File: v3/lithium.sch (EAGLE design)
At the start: 53 parts, among them J1 batt, J2 battery, J3 motor, U1 TPS61088VQFN20, U1_C22 8.2nF, U1_CBST 100nF, U1_CCOMP 680PF, U1_CCOMP2 36pF, U1_CIN 0.47uF, U1_CIN2 100nF, U1_COUT 0.47uF, U1_CVCC 1uF, U1_L1 DR73-1R0-R, U1_RCOMP 38.3K Ohms, U1_RFBB 118K Ohms, U1_RFBT 470K Ohms, U1_RLIM 102K Ohms, U1_RT 261K Ohms, U4 TPS2113APWR, U4_C3 0.1uF, U4_C4 0.1uF, U4_RPG 100K Ohms, U5 MCP73833-FCI/UN, U5_C1 1.0uF, U5_C2 1.0uF, U5_R1 1K Ohm, U6 TPS61230A, U6_CBST 10 nF, U6_CFF 10pF, U6_CIN 22uF, U6_COUT 22uF, U6_RFBB 100K Ohms, U6_RFBT 316K Ohms

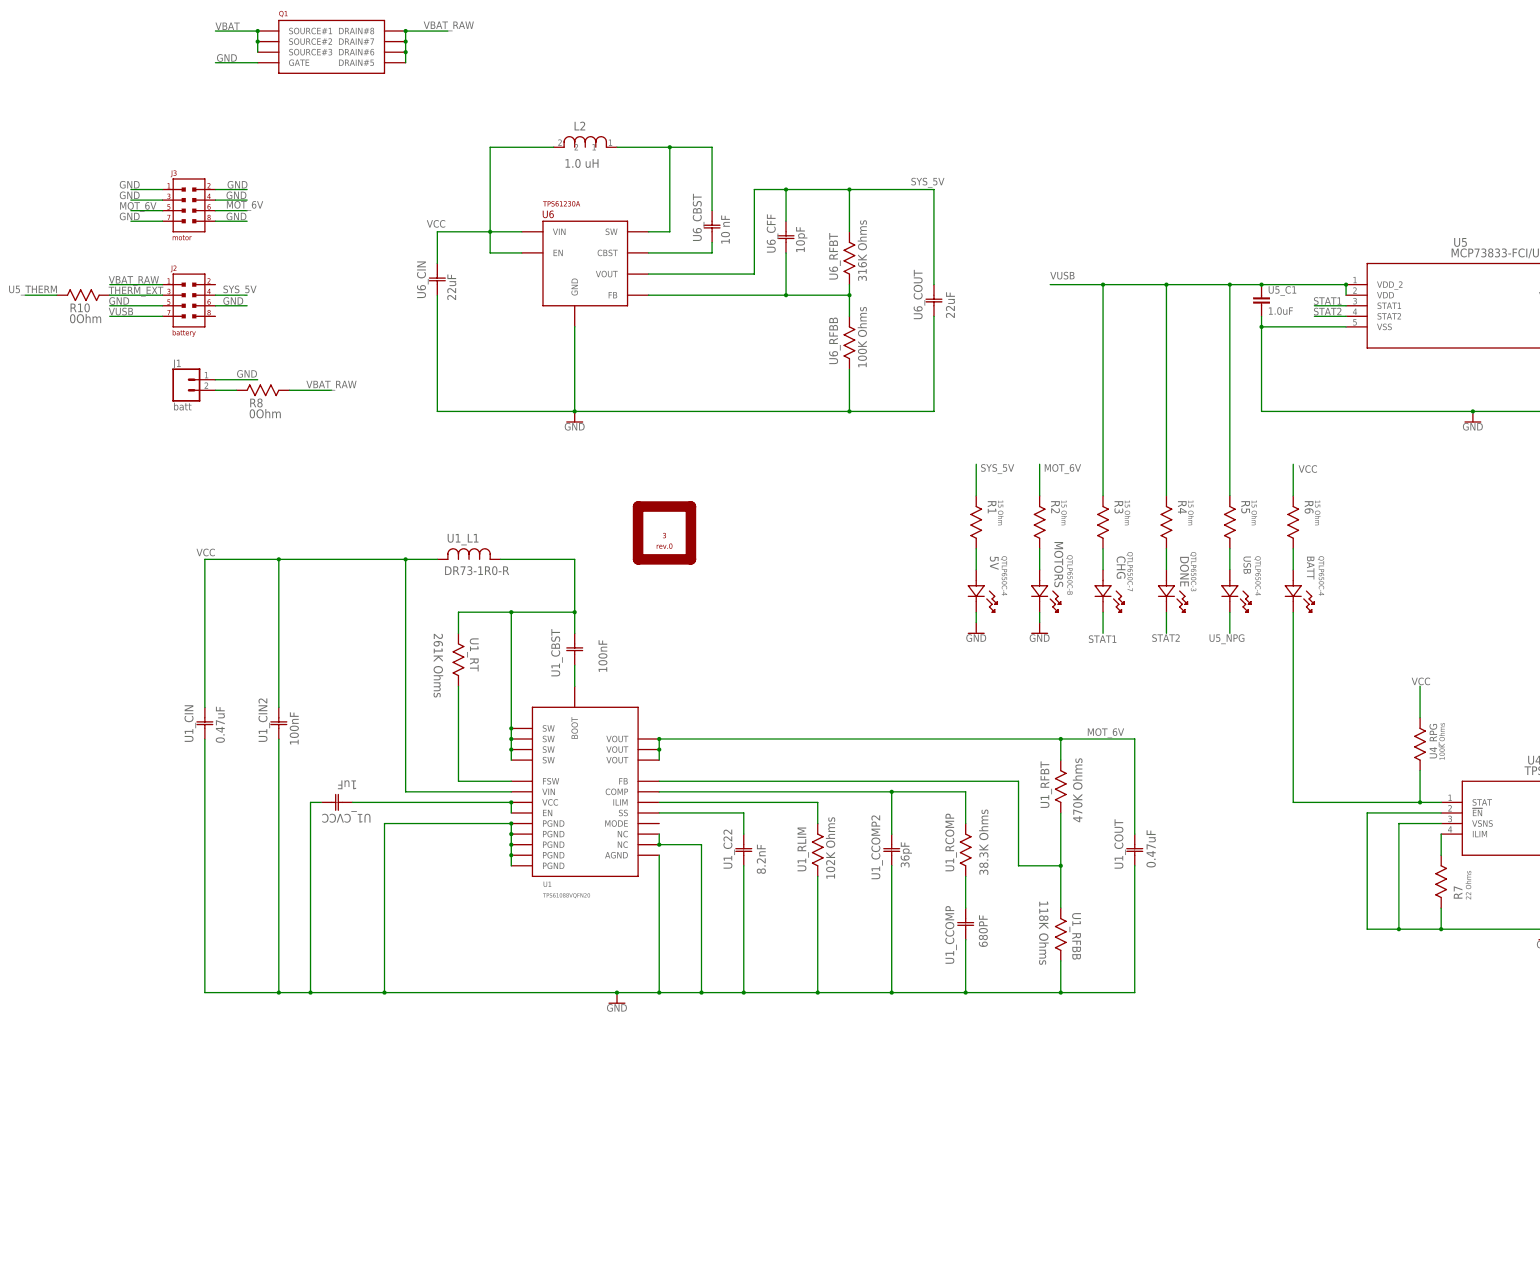
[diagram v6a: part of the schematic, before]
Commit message: Lithium with ATTiny84 for ADC.
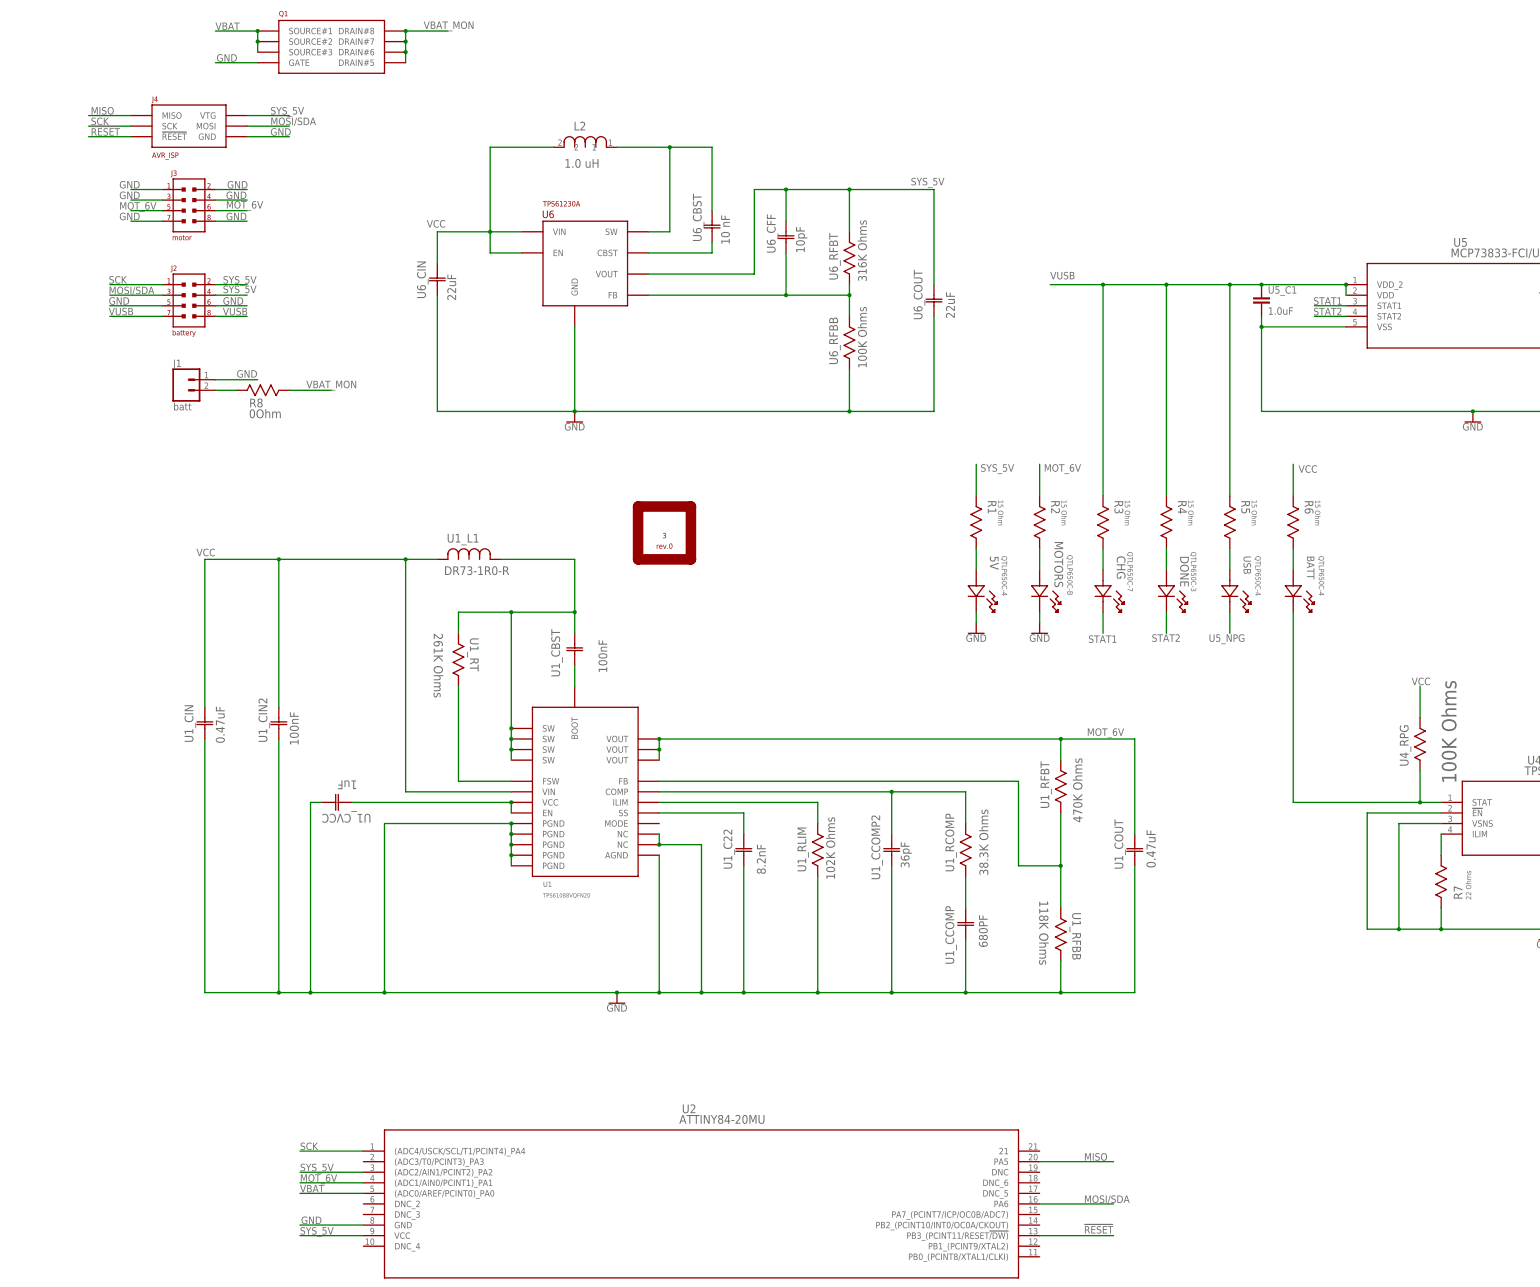
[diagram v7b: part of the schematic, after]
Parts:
- removed R10: 0Ohm, Vishay_By_element14_Batch_1:CRCW08050000Z0EB
- added J4: AVR_ISP, 32bits:AVR_ISP
- added U2: ATTINY84-20MU, 32bits:ATTINY84-20MU
- U4_RPG: device Vishay_By_element14_Batch_1:CRCW0603100KFKEA -> Vishay_By_element14_Batch_1:CRCW1206100KFKEA
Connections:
- removed net THERM_EXT: J2.3, R10.1
- removed net VBAT_RAW: J2.1, Q1.DRAIN#5, Q1.DRAIN#6, Q1.DRAIN#7, Q1.DRAIN#8, R8.1
- new net !RESET: J4.!RESET, U2.PB3_(PCINT11/RESET!/DW)
- new net MISO: J4.MISO, U2.PA5
- new net MOSI/SDA: J2.3, J4.MOSI, U2.PA6
- new net SCK: J2.1, J4.SCK, U2.(ADC4/USCK/SCL/T1/PCINT4)_PA4
- new net VBAT_MON: Q1.DRAIN#5, Q1.DRAIN#6, Q1.DRAIN#7, Q1.DRAIN#8, R8.1
- net GND: now also J4.GND, U2.GND
- net MOT_6V: now also U2.(ADC1/AIN0/PCINT1)_PA1
- net SYS_5V: now also J2.2, J4.VTG, U2.(ADC2/AIN1/PCINT2)_PA2, U2.VCC
- net U5_THERM: no longer R10.2
- net VBAT: now also U2.(ADC0/AREF/PCINT0)_PA0
- net VUSB: now also J2.8
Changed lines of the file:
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@@
 <part name="U4_C4" library="SparkFun-Capacitors" deviceset="0.1UF" device="-0402-16V-10%" value="0.1uF"/>
 <part name="BATT" library="Dialight_By_element14_Batch_1" deviceset="597-3311-407F" device="" value="QTLP650C-4"/>
-<part name="U4_RPG" library="Vishay_By_element14_Batch_1" deviceset="CRCW0603100KFKEA" device="" value="100K Ohms"/>
 <part name="U6" library="32bits" deviceset="TPS61230A" device=""/>
 <part name="L2" library="Bourns_By_element14_Batch_1" deviceset="PM1210-1R0J-RC" device="" value="1.0 uH"/>
@@
 <part name="S1" library="32bits" deviceset="SS312SAH4" device=""/>
 <part name="Q1" library="32bits" deviceset="SI7137DP" device=""/>
-<part name="R10" library="Vishay_By_element14_Batch_1" deviceset="CRCW08050000Z0EB" device="" value="0Ohm"/>
+<part name="U2" library="32bits" deviceset="ATTINY84-20MU" device=""/>
+<part name="J4" library="32bits" deviceset="AVR_ISP" device=""/>
+<part name="U4_RPG" library="Vishay_By_element14_Batch_1" deviceset="CRCW1206100KFKEA" device="" value="100K Ohms"/>
 </parts>
 <sheets>
@@
 <attribute name="NAME" x="264.922" y="105.0036" size="1.778" layer="95" ratio="10" rot="SR270"/>
 </instance>
-<instance part="U4_RPG" gate="A" x="292.1" y="53.34" smashed="yes" rot="R90">
-<attribute name="VALUE" x="298.0436" y="55.8038" size="1.27" layer="96" ratio="10" rot="SR90"/>
-<attribute name="NAME" x="296.1894" y="56.1086" size="1.778" layer="95" ratio="10" rot="SR90"/>
-</instance>
 <instance part="U6" gate="G$1" x="81.28" y="185.42"/>
 <instance part="L2" gate="A" x="83.82" y="203.2" smashed="yes">
@@
 <instance part="S1" gate="G$1" x="363.22" y="58.42" rot="R90"/>
 <instance part="Q1" gate="G$1" x="17.78" y="233.68"/>
-<instance part="R10" gate="A" x="-35.56" y="167.64" smashed="yes">
-<attribute name="VALUE" x="-32.5882" y="160.9344" size="2.1082" layer="96" ratio="10" rot="SR0"/>
-<attribute name="NAME" x="-32.5374" y="163.5506" size="2.0828" layer="95" ratio="10" rot="SR0"/>
-</instance>
+<instance part="U2" gate="A" x="35.56" y="-38.1"/>
+<instance part="J4" gate="A" x="-12.7" y="213.36"/>
+<instance part="U4_RPG" gate="A" x="292.1" y="53.34" rot="R90"/>
 </instances>
 <busses>
@@
 <label x="5.08" y="190.754" size="1.778" layer="95"/>
 </segment>
+<segment>
+<pinref part="U2" gate="A" pin="GND"/>
+<wire x1="38.1" y1="-55.88" x2="22.86" y2="-55.88" width="0.1524" layer="91"/>
+<label x="23.114" y="-55.626" size="1.778" layer="95"/>
+</segment>
+<segment>
+<pinref part="J4" gate="A" pin="GND"/>
+<wire x1="10.16" y1="205.74" x2="20.32" y2="205.74" width="0.1524" layer="91"/>
+<label x="15.748" y="205.994" size="1.778" layer="95"/>
+</segment>
 </net>
 <net name="SW" class="0">
@@
 </segment>
 <segment>
-<pinref part="U4_RPG" gate="A" pin="1"/>
 <wire x1="292.1" y1="66.04" x2="292.1" y2="73.66" width="0.1524" layer="91"/>
 <label x="290.068" y="73.914" size="1.778" layer="95"/>
+<pinref part="U4_RPG" gate="A" pin="1"/>
 </segment>
 <segment>
@@
 <label x="5.08" y="188.468" size="1.778" layer="95"/>
 </segment>
+<segment>
+<pinref part="U2" gate="A" pin="(ADC1/AIN0/PCINT1)_PA1"/>
+<wire x1="38.1" y1="-45.72" x2="22.86" y2="-45.72" width="0.1524" layer="91"/>
+<label x="22.86" y="-45.466" size="1.778" layer="95"/>
+</segment>
 </net>
 <net name="VBAT" class="0">
@@
 <junction x="12.7" y="231.14"/>
 <label x="2.54" y="231.394" size="1.778" layer="95"/>
+</segment>
+<segment>
+<pinref part="U2" gate="A" pin="(ADC0/AREF/PCINT0)_PA0"/>
+<wire x1="38.1" y1="-48.26" x2="22.86" y2="-48.26" width="0.1524" layer="91"/>
+<label x="22.86" y="-48.006" size="1.778" layer="95"/>
 </segment>
 </net>
@@
 <label x="-23.114" y="162.814" size="1.778" layer="95"/>
 </segment>
+<segment>
+<pinref part="J2" gate="A" pin="8"/>
+<wire x1="2.54" y1="162.56" x2="10.16" y2="162.56" width="0.1524" layer="91"/>
+<label x="4.318" y="162.814" size="1.778" layer="95"/>
+</segment>
 </net>
 <net name="U5_PROG" class="0">
@@
 <pinref part="U4" gate="A" pin="STAT"/>
 <wire x1="297.18" y1="45.72" x2="292.1" y2="45.72" width="0.1524" layer="91"/>
-<pinref part="U4_RPG" gate="A" pin="2"/>
 <wire x1="292.1" y1="53.34" x2="292.1" y2="45.72" width="0.1524" layer="91"/>
 <wire x1="261.62" y1="45.72" x2="292.1" y2="45.72" width="0.1524" layer="91"/>
 <junction x="292.1" y="45.72"/>
+<pinref part="U4_RPG" gate="A" pin="2"/>
 </segment>
 </net>
@@
 <label x="4.318" y="168.148" size="1.778" layer="95"/>
 </segment>
+<segment>
+<pinref part="J2" gate="A" pin="2"/>
+<wire x1="2.54" y1="170.18" x2="10.16" y2="170.18" width="0.1524" layer="91"/>
+<label x="4.318" y="170.434" size="1.778" layer="95"/>
+</segment>
+<segment>
+<pinref part="U2" gate="A" pin="VCC"/>
+<wire x1="38.1" y1="-58.42" x2="22.86" y2="-58.42" width="0.1524" layer="91"/>
+<label x="22.86" y="-58.166" size="1.778" layer="95"/>
+</segment>
+<segment>
+<pinref part="U2" gate="A" pin="(ADC2/AIN1/PCINT2)_PA2"/>
+<wire x1="38.1" y1="-43.18" x2="22.86" y2="-43.18" width="0.1524" layer="91"/>
+<label x="22.86" y="-42.926" size="1.778" layer="95"/>
+</segment>
+<segment>
+<pinref part="J4" gate="A" pin="VTG"/>
+<wire x1="10.16" y1="210.82" x2="20.32" y2="210.82" width="0.1524" layer="91"/>
+<label x="15.748" y="211.074" size="1.778" layer="95"/>
+</segment>
 </net>
 <net name="U1_VCC" class="0">
@@
 <wire x1="355.6" y1="165.1" x2="355.6" y2="157.48" width="0.1524" layer="91"/>
 </segment>
-<segment>
-<pinref part="R10" gate="A" pin="2"/>
-<wire x1="-35.56" y1="167.64" x2="-43.18" y2="167.64" width="0.1524" layer="91"/>
-<label x="-47.244" y="168.148" size="1.778" layer="95"/>
-</segment>
 </net>
 <net name="U4_ILIM" class="0">
@@
 </segment>
 </net>
-<net name="VBAT_RAW" class="0">
+<net name="VBAT_MON" class="0">
 <segment>
 <pinref part="Q1" gate="G$1" pin="DRAIN#5"/>
@@
 </segment>
 <segment>
+<pinref part="R8" gate="A" pin="1"/>
+<wire x1="20.32" y1="144.78" x2="30.48" y2="144.78" width="0.1524" layer="91"/>
+<label x="24.384" y="145.288" size="1.778" layer="95"/>
+</segment>
+</net>
+<net name="SCK" class="0">
+<segment>
+<pinref part="U2" gate="A" pin="(ADC4/USCK/SCL/T1/PCINT4)_PA4"/>
+<wire x1="38.1" y1="-38.1" x2="22.86" y2="-38.1" width="0.1524" layer="91"/>
+<label x="22.86" y="-37.846" size="1.778" layer="95"/>
+</segment>
+<segment>
+<pinref part="J4" gate="A" pin="SCK"/>
+<wire x1="-17.78" y1="208.28" x2="-27.94" y2="208.28" width="0.1524" layer="91"/>
+<label x="-27.432" y="208.534" size="1.778" layer="95"/>
+</segment>
+<segment>
 <pinref part="J2" gate="A" pin="1"/>
 <wire x1="-10.16" y1="170.18" x2="-22.86" y2="170.18" width="0.1524" layer="91"/>
 <label x="-23.114" y="170.434" size="1.778" layer="95"/>
 </segment>
-<segment>
-<pinref part="R8" gate="A" pin="1"/>
-<wire x1="20.32" y1="144.78" x2="30.48" y2="144.78" width="0.1524" layer="91"/>
-<label x="24.384" y="145.288" size="1.778" layer="95"/>
-</segment>
-</net>
-<net name="THERM_EXT" class="0">
+</net>
+<net name="!RESET" class="0">
+<segment>
+<pinref part="U2" gate="A" pin="PB3_(PCINT11/RESET!/DW)"/>
+<wire x1="200.66" y1="-58.42" x2="218.44" y2="-58.42" width="0.1524" layer="91"/>
+<label x="211.328" y="-57.912" size="1.778" layer="95"/>
+</segment>
+<segment>
+<pinref part="J4" gate="A" pin="!RESET"/>
+<wire x1="-17.78" y1="205.74" x2="-27.94" y2="205.74" width="0.1524" layer="91"/>
+<label x="-27.432" y="205.994" size="1.778" layer="95"/>
+</segment>
+</net>
+<net name="MOSI/SDA" class="0">
+<segment>
+<pinref part="U2" gate="A" pin="PA6"/>
+<wire x1="200.66" y1="-50.8" x2="218.44" y2="-50.8" width="0.1524" layer="91"/>
+<label x="211.328" y="-50.546" size="1.778" layer="95"/>
+</segment>
+<segment>
+<pinref part="J4" gate="A" pin="MOSI"/>
+<wire x1="10.16" y1="208.28" x2="20.32" y2="208.28" width="0.1524" layer="91"/>
+<label x="15.748" y="208.534" size="1.778" layer="95"/>
+</segment>
 <segment>
 <pinref part="J2" gate="A" pin="3"/>
 <wire x1="-10.16" y1="167.64" x2="-22.86" y2="167.64" width="0.1524" layer="91"/>
 <label x="-23.114" y="167.894" size="1.778" layer="95"/>
-<pinref part="R10" gate="A" pin="1"/>
-</segment>
-</net>
+</segment>
+</net>
+<net name="MISO" class="0">
+<segment>
+<pinref part="U2" gate="A" pin="PA5"/>
+<wire x1="200.66" y1="-40.64" x2="218.44" y2="-40.64" width="0.1524" layer="91"/>
+<label x="211.328" y="-40.386" size="1.778" layer="95"/>
+</segment>
+<segment>
+<pinref part="J4" gate="A" pin="MISO"/>
+<wire x1="-17.78" y1="210.82" x2="-27.94" y2="210.82" width="0.1524" layer="91"/>
+<label x="-27.432" y="211.074" size="1.778" layer="95"/>
+</segment>
+</net>
